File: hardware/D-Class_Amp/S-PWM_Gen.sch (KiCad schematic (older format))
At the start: 10 parts, among them U201 Opamp_Dual_Generic, U202 Comparator_Dual_Generic

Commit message: edits
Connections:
- net GNDS renamed -5V
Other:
- note added: "25kHz Triangle Wave Generation"
- note added: "S-PWM Inverting and Non-inverting outputs"
- moved on the sheet: C201, C202, C203, R201, R202, R203, R204, R205, U201A, U201B, U201C, U202A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

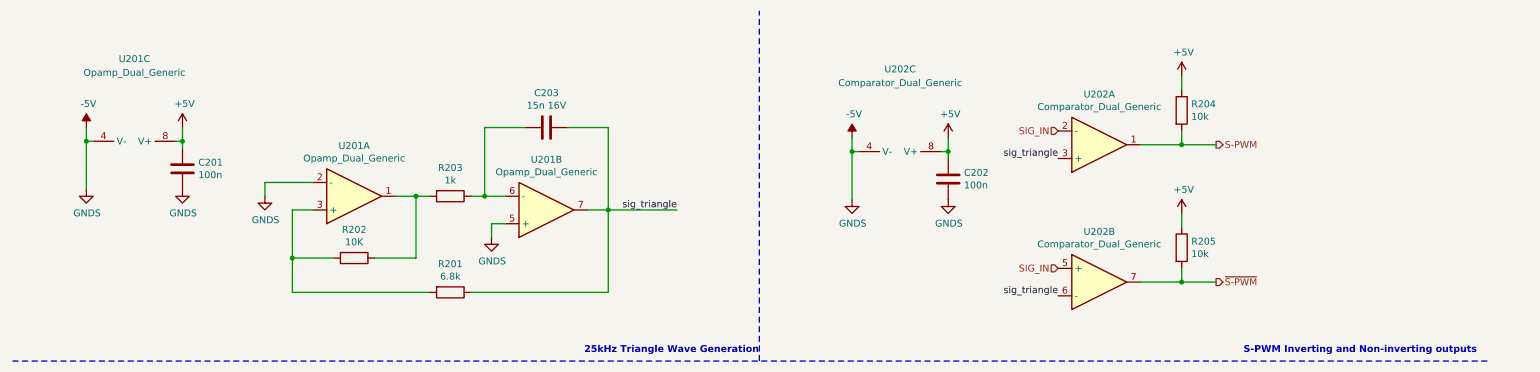
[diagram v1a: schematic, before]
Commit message: Added an input barel jack
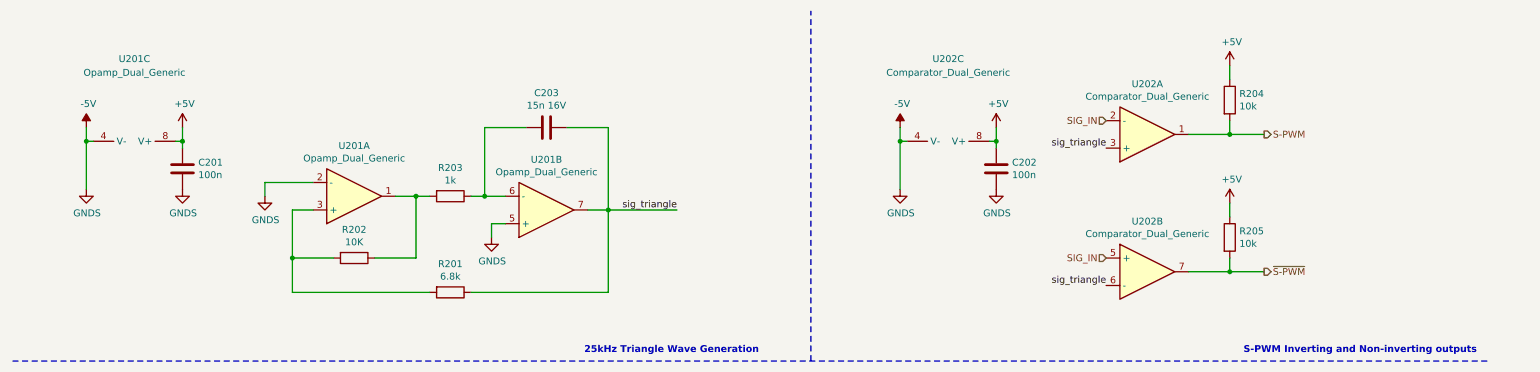
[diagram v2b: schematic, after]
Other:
- moved on the sheet: C202, R204, R205, U202A, U202B, U202C
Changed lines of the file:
@@
 Text Label 5325 1925 2    50   ~ 0
 sig_triangle
-Text HLabel 9250 1450 2    50   Output ~ 0
+Text HLabel 9600 1375 2    50   Output ~ 0
 S-PWM
-Text HLabel 9250 2450 2    50   Output ~ 0
+Text HLabel 9600 2375 2    50   Output ~ 0
 ~S-PWM
 $Comp
 L Device:Opamp_Dual_Generic U202
 U 1 1 610E84D1
-P 8400 1450
-F 0 "U202" H 8400 1083 50  0000 C CNN
-F 1 "Comparator_Dual_Generic" H 8400 1174 50  0000 C CNN
-F 2 "" H 8400 1450 50  0001 C CNN
-F 3 "~" H 8400 1450 50  0001 C CNN
-	1    8400 1450
+P 8750 1375
+F 0 "U202" H 8750 1008 50  0000 C CNN
+F 1 "Comparator_Dual_Generic" H 8750 1099 50  0000 C CNN
+F 2 "" H 8750 1375 50  0001 C CNN
+F 3 "~" H 8750 1375 50  0001 C CNN
+	1    8750 1375
 	1    0    0    1
 $EndComp
@@
 L Device:Opamp_Dual_Generic U202
 U 2 1 610E8A2F
-P 8400 2450
-F 0 "U202" H 8400 2817 50  0000 C CNN
-F 1 "Comparator_Dual_Generic" H 8400 2726 50  0000 C CNN
-F 2 "" H 8400 2450 50  0001 C CNN
-F 3 "~" H 8400 2450 50  0001 C CNN
-	2    8400 2450
+P 8750 2375
+F 0 "U202" H 8750 2742 50  0000 C CNN
+F 1 "Comparator_Dual_Generic" H 8750 2651 50  0000 C CNN
+F 2 "" H 8750 2375 50  0001 C CNN
+F 3 "~" H 8750 2375 50  0001 C CNN
+	2    8750 2375
 	1    0    0    -1
 $EndComp
@@
 L Device:C C202
 U 1 1 610E9B40
-P 7300 1700
-F 0 "C202" H 7415 1746 50  0000 L CNN
-F 1 "100n" H 7415 1655 50  0000 L CNN
-F 2 "" H 7338 1550 50  0001 C CNN
-F 3 "~" H 7300 1700 50  0001 C CNN
-	1    7300 1700
+P 7650 1625
+F 0 "C202" H 7765 1671 50  0000 L CNN
+F 1 "100n" H 7765 1580 50  0000 L CNN
+F 2 "" H 7688 1475 50  0001 C CNN
+F 3 "~" H 7650 1625 50  0001 C CNN
+	1    7650 1625
 	1    0    0    -1
 $EndComp
@@
 L Device:Opamp_Dual_Generic U202
 U 3 1 610E9B4A
-P 6950 1600
-F 0 "U202" V 6250 1600 50  0000 C CNN
-F 1 "Comparator_Dual_Generic" V 6350 1600 50  0000 C CNN
-F 2 "" H 6950 1600 50  0001 C CNN
-F 3 "~" H 6950 1600 50  0001 C CNN
-	3    6950 1600
+P 7300 1525
+F 0 "U202" V 6600 1525 50  0000 C CNN
+F 1 "Comparator_Dual_Generic" V 6700 1525 50  0000 C CNN
+F 2 "" H 7300 1525 50  0001 C CNN
+F 3 "~" H 7300 1525 50  0001 C CNN
+	3    7300 1525
 	0    1    1    0
 $EndComp
 Wire Wire Line
-	7300 1550 7300 1500
-Wire Wire Line
-	7250 1500 7300 1500
-Wire Wire Line
-	6600 1500 6650 1500
+	7650 1475 7650 1425
+Wire Wire Line
+	7600 1425 7650 1425
+Wire Wire Line
+	6950 1425 7000 1425
 $Comp
 L power:+5V #PWR?
 U 1 1 610E9B57
-P 7300 1400
-F 0 "#PWR?" H 7300 1250 50  0001 C CNN
-F 1 "+5V" H 7315 1573 50  0000 C CNN
-F 2 "" H 7300 1400 50  0001 C CNN
-F 3 "" H 7300 1400 50  0001 C CNN
-	1    7300 1400
-	1    0    0    -1
-$EndComp
-Wire Wire Line
-	7300 1400 7300 1500
-Connection ~ 7300 1500
+P 7650 1325
+F 0 "#PWR?" H 7650 1175 50  0001 C CNN
+F 1 "+5V" H 7665 1498 50  0000 C CNN
+F 2 "" H 7650 1325 50  0001 C CNN
+F 3 "" H 7650 1325 50  0001 C CNN
+	1    7650 1325
+	1    0    0    -1
+$EndComp
+Wire Wire Line
+	7650 1325 7650 1425
+Connection ~ 7650 1425
 $Comp
 L power:GNDS #PWR?
 U 1 1 610E9B63
-P 7300 1850
-F 0 "#PWR?" H 7300 1600 50  0001 C CNN
-F 1 "GNDS" H 7305 1677 50  0000 C CNN
-F 2 "" H 7300 1850 50  0001 C CNN
-F 3 "" H 7300 1850 50  0001 C CNN
-	1    7300 1850
+P 7650 1775
+F 0 "#PWR?" H 7650 1525 50  0001 C CNN
+F 1 "GNDS" H 7655 1602 50  0000 C CNN
+F 2 "" H 7650 1775 50  0001 C CNN
+F 3 "" H 7650 1775 50  0001 C CNN
+	1    7650 1775
 	1    0    0    -1
 $EndComp
@@
 L power:GNDS #PWR?
 U 1 1 610E9B6D
-P 6600 1850
-F 0 "#PWR?" H 6600 1600 50  0001 C CNN
-F 1 "GNDS" H 6605 1677 50  0000 C CNN
-F 2 "" H 6600 1850 50  0001 C CNN
-F 3 "" H 6600 1850 50  0001 C CNN
-	1    6600 1850
-	1    0    0    -1
-$EndComp
-Wire Wire Line
-	6600 1850 6600 1500
-Text HLabel 8100 2350 0    50   Input ~ 0
+P 6950 1775
+F 0 "#PWR?" H 6950 1525 50  0001 C CNN
+F 1 "GNDS" H 6955 1602 50  0000 C CNN
+F 2 "" H 6950 1775 50  0001 C CNN
+F 3 "" H 6950 1775 50  0001 C CNN
+	1    6950 1775
+	1    0    0    -1
+$EndComp
+Wire Wire Line
+	6950 1775 6950 1425
+Text HLabel 8450 2275 0    50   Input ~ 0
 SIG_IN
-Text HLabel 8100 1350 0    50   Input ~ 0
+Text HLabel 8450 1275 0    50   Input ~ 0
 SIG_IN
-Text Label 8100 1550 2    50   ~ 0
+Text Label 8450 1475 2    50   ~ 0
 sig_triangle
-Text Label 8100 2550 2    50   ~ 0
+Text Label 8450 2475 2    50   ~ 0
 sig_triangle
 Wire Wire Line
-	8700 1450 9000 1450
+	9050 1375 9350 1375
 $Comp
 L Device:R R204
 U 1 1 6112AEF0
-P 9000 1200
-F 0 "R204" H 9070 1246 50  0000 L CNN
-F 1 "10k" H 9070 1155 50  0000 L CNN
-F 2 "" V 8930 1200 50  0001 C CNN
-F 3 "~" H 9000 1200 50  0001 C CNN
-	1    9000 1200
-	1    0    0    -1
-$EndComp
-Wire Wire Line
-	9000 1350 9000 1450
-Connection ~ 9000 1450
-Wire Wire Line
-	9000 1450 9250 1450
+P 9350 1125
+F 0 "R204" H 9420 1171 50  0000 L CNN
+F 1 "10k" H 9420 1080 50  0000 L CNN
+F 2 "" V 9280 1125 50  0001 C CNN
+F 3 "~" H 9350 1125 50  0001 C CNN
+	1    9350 1125
+	1    0    0    -1
+$EndComp
+Wire Wire Line
+	9350 1275 9350 1375
+Connection ~ 9350 1375
+Wire Wire Line
+	9350 1375 9600 1375
 $Comp
 L power:+5V #PWR?
 U 1 1 61133A73
-P 9000 950
-F 0 "#PWR?" H 9000 800 50  0001 C CNN
-F 1 "+5V" H 9015 1123 50  0000 C CNN
-F 2 "" H 9000 950 50  0001 C CNN
-F 3 "" H 9000 950 50  0001 C CNN
-	1    9000 950
-	1    0    0    -1
-$EndComp
-Wire Wire Line
-	9000 950  9000 1050
-Wire Wire Line
-	8700 2450 9000 2450
+P 9350 875
+F 0 "#PWR?" H 9350 725 50  0001 C CNN
+F 1 "+5V" H 9365 1048 50  0000 C CNN
+F 2 "" H 9350 875 50  0001 C CNN
+F 3 "" H 9350 875 50  0001 C CNN
+	1    9350 875
+	1    0    0    -1
+$EndComp
+Wire Wire Line
+	9350 875  9350 975
+Wire Wire Line
+	9050 2375 9350 2375
 $Comp
 L Device:R R205
 U 1 1 61138A41
-P 9000 2200
-F 0 "R205" H 9070 2246 50  0000 L CNN
-F 1 "10k" H 9070 2155 50  0000 L CNN
-F 2 "" V 8930 2200 50  0001 C CNN
-F 3 "~" H 9000 2200 50  0001 C CNN
-	1    9000 2200
-	1    0    0    -1
-$EndComp
-Wire Wire Line
-	9000 2350 9000 2450
-Connection ~ 9000 2450
-Wire Wire Line
-	9000 2450 9250 2450
+P 9350 2125
+F 0 "R205" H 9420 2171 50  0000 L CNN
+F 1 "10k" H 9420 2080 50  0000 L CNN
+F 2 "" V 9280 2125 50  0001 C CNN
+F 3 "~" H 9350 2125 50  0001 C CNN
+	1    9350 2125
+	1    0    0    -1
+$EndComp
+Wire Wire Line
+	9350 2275 9350 2375
+Connection ~ 9350 2375
+Wire Wire Line
+	9350 2375 9600 2375
 $Comp
 L power:+5V #PWR?
 U 1 1 61138A4E
-P 9000 1950
-F 0 "#PWR?" H 9000 1800 50  0001 C CNN
-F 1 "+5V" H 9015 2123 50  0000 C CNN
-F 2 "" H 9000 1950 50  0001 C CNN
-F 3 "" H 9000 1950 50  0001 C CNN
-	1    9000 1950
-	1    0    0    -1
-$EndComp
-Wire Wire Line
-	9000 1950 9000 2050
+P 9350 1875
+F 0 "#PWR?" H 9350 1725 50  0001 C CNN
+F 1 "+5V" H 9365 2048 50  0000 C CNN
+F 2 "" H 9350 1875 50  0001 C CNN
+F 3 "" H 9350 1875 50  0001 C CNN
+	1    9350 1875
+	1    0    0    -1
+$EndComp
+Wire Wire Line
+	9350 1875 9350 1975
 $Comp
 L power:-5V #PWR?
@@
 L power:-5V #PWR?
 U 1 1 611AED99
-P 6600 1400
-F 0 "#PWR?" H 6600 1500 50  0001 C CNN
-F 1 "-5V" H 6615 1573 50  0000 C CNN
-F 2 "" H 6600 1400 50  0001 C CNN
-F 3 "" H 6600 1400 50  0001 C CNN
-	1    6600 1400
-	1    0    0    -1
-$EndComp
-Wire Wire Line
-	6600 1400 6600 1500
-Connection ~ 6600 1500
+P 6950 1325
+F 0 "#PWR?" H 6950 1425 50  0001 C CNN
+F 1 "-5V" H 6965 1498 50  0000 C CNN
+F 2 "" H 6950 1325 50  0001 C CNN
+F 3 "" H 6950 1325 50  0001 C CNN
+	1    6950 1325
+	1    0    0    -1
+$EndComp
+Wire Wire Line
+	6950 1325 6950 1425
+Connection ~ 6950 1425
 Wire Notes Line
 	11225 3025 475  3025
-Wire Notes Line
-	5925 3025 5925 475
 Text Notes 4650 2975 0    50   ~ 10
 25kHz Triangle Wave Generation
 Text Notes 9450 2975 0    50   ~ 10
 S-PWM Inverting and Non-inverting outputs
+Wire Notes Line
+	6300 3025 6300 475
 $EndSCHEMATC

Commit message: update the letspice model so that the trianlge wave goes from rail to rail. Also added a potentiometer to the feedback path of the triangle wave generator, allowing for precise tuning of this gain.
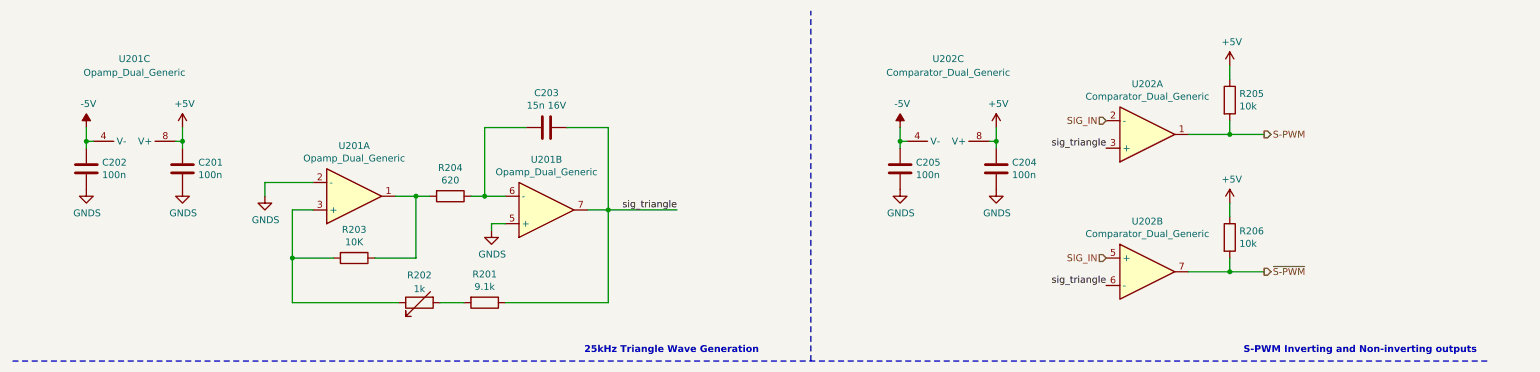
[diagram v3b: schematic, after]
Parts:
- added C202, C205: 100n, symbol Device:C
- added R202: 1k, symbol Device:R_Variable
- R201: value 6.8k -> 9.1k
- R204: renamed from R203; value 1k -> 620
- renumbered C202 to C204, R202 to R203, R204 to R205, R205 to R206
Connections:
- net -5V: now also C202.1, C205.1; no longer C201.2, C204.2, U201.2 (-), U201.5 (+)
- net at R203.2, U201.3 (+): now also R202.1; no longer R201.2
- new net: R201.2, R202.2
- new net GNDS: C201.2, C202.2, C204.2, C205.2, U201.2 (-), U201.5 (+)
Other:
- moved on the sheet: R201
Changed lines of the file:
@@
 $Descr A4 11693 8268
 encoding utf-8
-Sheet 5 5
-Title ""
+Sheet 1 1
+Title "S-PWM Generator "
 Date ""
 Rev ""
@@
 $EndComp
 $Comp
-L Device:R R202
+L Device:R R203
 U 1 1 61054D4F
 P 2975 2275
-F 0 "R202" V 2768 2275 50  0000 C CNN
+F 0 "R203" V 2768 2275 50  0000 C CNN
 F 1 "10K" V 2859 2275 50  0000 C CNN
 F 2 "" V 2905 2275 50  0001 C CNN
@@
 $EndComp
 $Comp
-L Device:R R201
-U 1 1 61055E03
-P 3675 2525
-F 0 "R201" V 3468 2525 50  0000 C CNN
-F 1 "6.8k" V 3559 2525 50  0000 C CNN
-F 2 "" V 3605 2525 50  0001 C CNN
-F 3 "~" H 3675 2525 50  0001 C CNN
-	1    3675 2525
-	0    1    1    0
-$EndComp
-$Comp
-L Device:R R203
+L Device:R R204
 U 1 1 610560D6
 P 3675 1825
-F 0 "R203" V 3468 1825 50  0000 C CNN
-F 1 "1k" V 3559 1825 50  0000 C CNN
+F 0 "R204" V 3468 1825 50  0000 C CNN
+F 1 "620" V 3559 1825 50  0000 C CNN
 F 2 "" V 3605 1825 50  0001 C CNN
 F 3 "~" H 3675 1825 50  0001 C CNN
@@
 Wire Wire Line
 	2525 1925 2675 1925
-Wire Wire Line
-	3525 2525 2525 2525
-Wire Wire Line
-	2525 2525 2525 2275
 Connection ~ 2525 2275
 Wire Wire Line
-	3825 2525 4825 2525
-Wire Wire Line
 	4675 1925 4825 1925
-Wire Wire Line
-	4825 1925 4825 2525
 $Comp
 L power:GNDS #PWR?
@@
 L power:GNDS #PWR?
 U 1 1 61065BCC
-P 3975 2125
-F 0 "#PWR?" H 3975 1875 50  0001 C CNN
-F 1 "GNDS" H 3980 1952 50  0000 C CNN
-F 2 "" H 3975 2125 50  0001 C CNN
-F 3 "" H 3975 2125 50  0001 C CNN
-	1    3975 2125
-	1    0    0    -1
-$EndComp
-Wire Wire Line
-	3975 2125 3975 2025
+P 3975 2075
+F 0 "#PWR?" H 3975 1825 50  0001 C CNN
+F 1 "GNDS" H 3980 1902 50  0000 C CNN
+F 2 "" H 3975 2075 50  0001 C CNN
+F 3 "" H 3975 2075 50  0001 C CNN
+	1    3975 2075
+	1    0    0    -1
+$EndComp
+Wire Wire Line
+	3975 2075 3975 2025
 Wire Wire Line
 	3975 2025 4075 2025
@@
 	1    0    0    -1
 $EndComp
-Wire Wire Line
-	1025 1775 1025 1425
 Wire Wire Line
 	4825 1925 5325 1925
@@
 $EndComp
 $Comp
-L Device:C C202
+L Device:C C204
 U 1 1 610E9B40
 P 7650 1625
-F 0 "C202" H 7765 1671 50  0000 L CNN
+F 0 "C204" H 7765 1671 50  0000 L CNN
 F 1 "100n" H 7765 1580 50  0000 L CNN
 F 2 "" H 7688 1475 50  0001 C CNN
@@
 	1    0    0    -1
 $EndComp
-Wire Wire Line
-	6950 1775 6950 1425
 Text HLabel 8450 2275 0    50   Input ~ 0
 SIG_IN
@@
 	9050 1375 9350 1375
 $Comp
-L Device:R R204
+L Device:R R205
 U 1 1 6112AEF0
 P 9350 1125
-F 0 "R204" H 9420 1171 50  0000 L CNN
+F 0 "R205" H 9420 1171 50  0000 L CNN
 F 1 "10k" H 9420 1080 50  0000 L CNN
 F 2 "" V 9280 1125 50  0001 C CNN
@@
 	9050 2375 9350 2375
 $Comp
-L Device:R R205
+L Device:R R206
 U 1 1 61138A41
 P 9350 2125
-F 0 "R205" H 9420 2171 50  0000 L CNN
+F 0 "R206" H 9420 2171 50  0000 L CNN
 F 1 "10k" H 9420 2080 50  0000 L CNN
 F 2 "" V 9280 2125 50  0001 C CNN
@@
 	1    0    0    -1
 $EndComp
-Wire Wire Line
-	1025 1325 1025 1425
-Connection ~ 1025 1425
 $Comp
 L power:-5V #PWR?
@@
 Wire Wire Line
 	6950 1325 6950 1425
-Connection ~ 6950 1425
-Wire Notes Line
-	11225 3025 475  3025
-Text Notes 4650 2975 0    50   ~ 10
-25kHz Triangle Wave Generation
 Text Notes 9450 2975 0    50   ~ 10
 S-PWM Inverting and Non-inverting outputs
 Wire Notes Line
 	6300 3025 6300 475
+$Comp
+L Device:R R201
+U 1 1 61055E03
+P 3925 2600
+F 0 "R201" V 3718 2600 50  0000 C CNN
+F 1 "9.1k" V 3809 2600 50  0000 C CNN
+F 2 "" V 3855 2600 50  0001 C CNN
+F 3 "~" H 3925 2600 50  0001 C CNN
+	1    3925 2600
+	0    1    1    0
+$EndComp
+$Comp
+L Device:R_Variable R202
+U 1 1 6105EC41
+P 3450 2600
+F 0 "R202" V 3250 2600 50  0000 C CNN
+F 1 "1k" V 3350 2600 50  0000 C CNN
+F 2 "" V 3380 2600 50  0001 C CNN
+F 3 "~" H 3450 2600 50  0001 C CNN
+F 4 "CT6EP102" V 3450 2600 50  0001 C CNN "Part Number"
+	1    3450 2600
+	0    -1   1    0
+$EndComp
+Wire Wire Line
+	3775 2600 3600 2600
+Wire Wire Line
+	3300 2600 2525 2600
+Wire Wire Line
+	2525 2275 2525 2600
+Wire Wire Line
+	4075 2600 4825 2600
+Text Notes 4650 2975 0    50   ~ 10
+25kHz Triangle Wave Generation
+Wire Notes Line
+	11225 3025 475  3025
+Wire Wire Line
+	4825 1925 4825 2600
+$Comp
+L Device:C C202
+U 1 1 61084C95
+P 1025 1625
+F 0 "C202" H 1140 1671 50  0000 L CNN
+F 1 "100n" H 1140 1580 50  0000 L CNN
+F 2 "" H 1063 1475 50  0001 C CNN
+F 3 "~" H 1025 1625 50  0001 C CNN
+	1    1025 1625
+	1    0    0    -1
+$EndComp
+Wire Wire Line
+	1025 1325 1025 1425
+Wire Wire Line
+	1025 1475 1025 1425
+Connection ~ 1025 1425
+$Comp
+L Device:C C205
+U 1 1 61090BA0
+P 6950 1625
+F 0 "C205" H 7065 1671 50  0000 L CNN
+F 1 "100n" H 7065 1580 50  0000 L CNN
+F 2 "" H 6988 1475 50  0001 C CNN
+F 3 "~" H 6950 1625 50  0001 C CNN
+	1    6950 1625
+	1    0    0    -1
+$EndComp
+Wire Wire Line
+	6950 1475 6950 1425
+Connection ~ 6950 1425
 $EndSCHEMATC
